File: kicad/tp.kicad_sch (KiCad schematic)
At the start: 11 parts, among them SW1 SWITCH_MODE, SW2 ALARM_OFF, U1 STM32F103RBTx

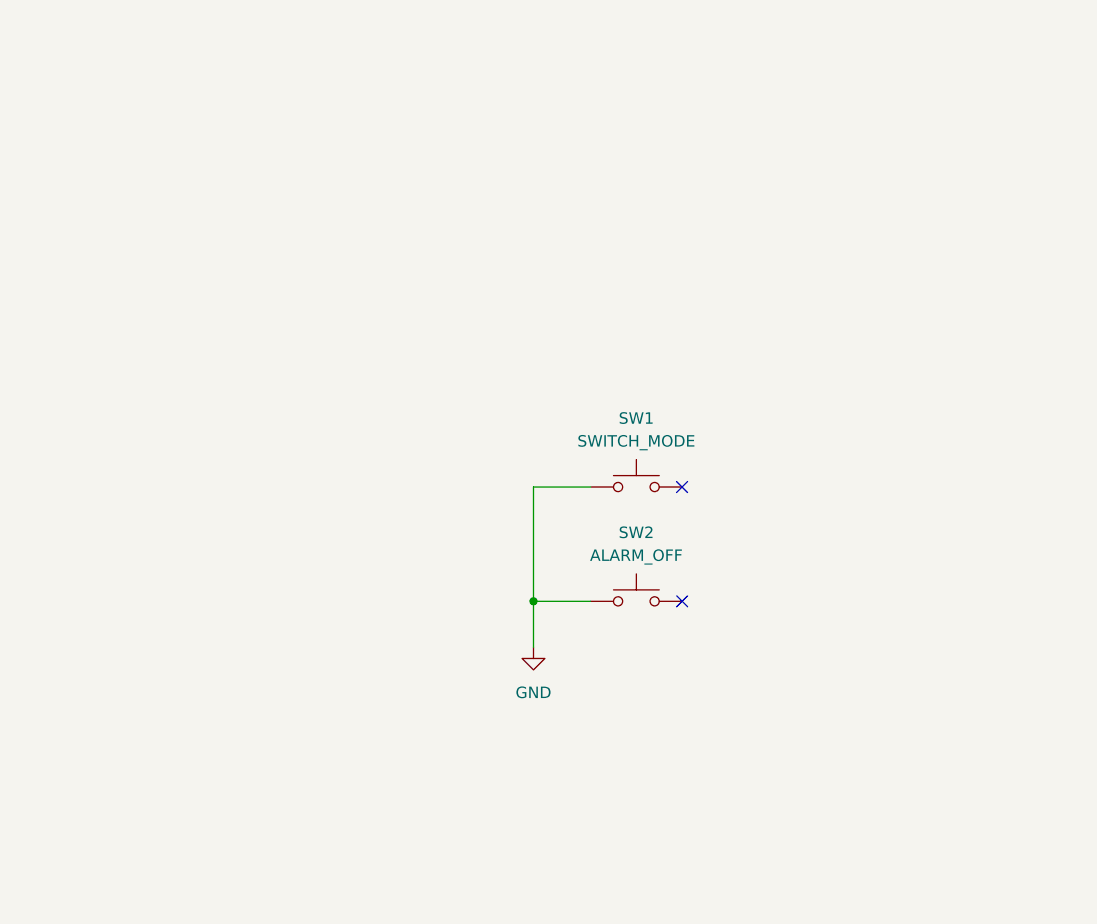
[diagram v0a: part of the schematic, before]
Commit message: feat(sch): agrega display lcd
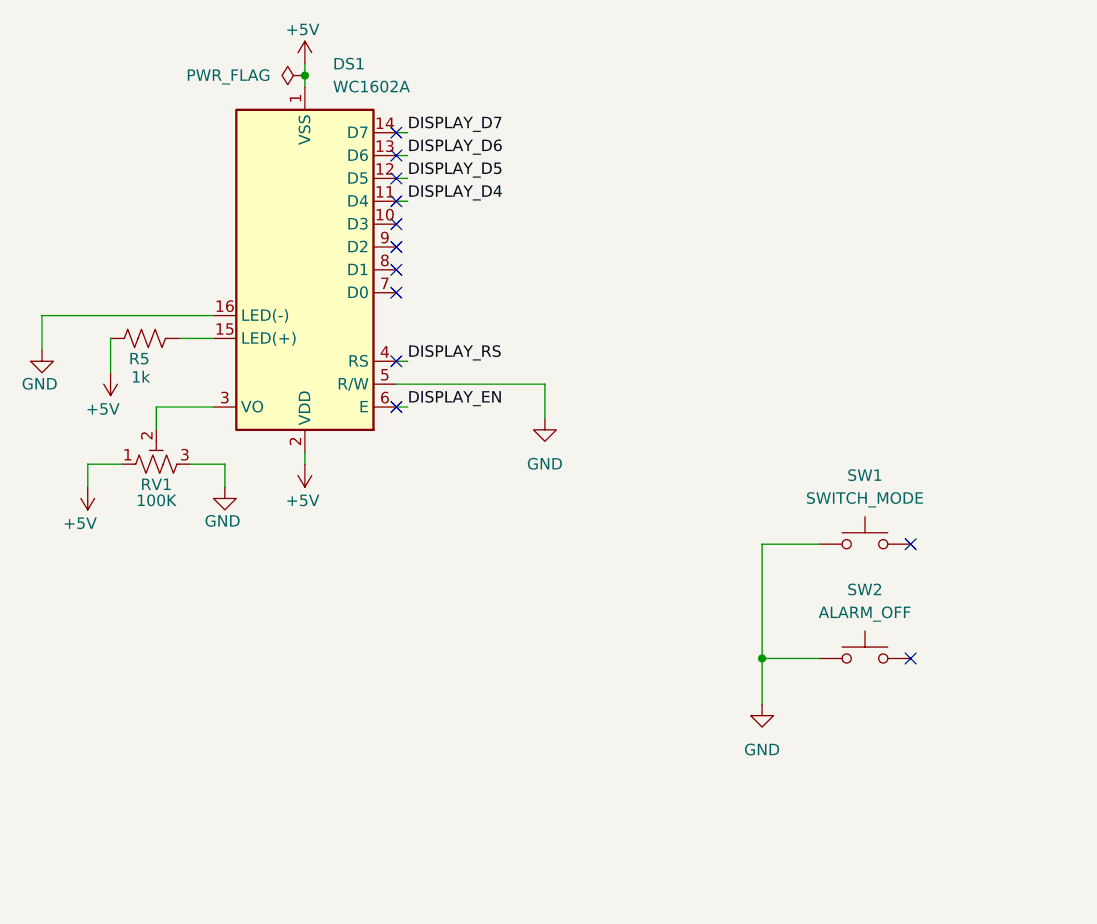
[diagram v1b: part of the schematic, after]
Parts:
- added DS1: WC1602A, Display:WC1602A, symbol Display_Character:WC1602A
- added R5: 1k, symbol Device:R_US
- added RV1: 100K, symbol Device:R_Potentiometer_Trim_US
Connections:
- net GND: now also DS1.16 (LED(-)), DS1.5 (R/W), RV1.3
- new net: DS1.15 (LED(+)), R5.1
- new net: DS1.3 (VO), RV1.2
- new net +5V: DS1.1 (VSS), DS1.2 (VDD), R5.2, RV1.1
- new net DISPLAY_D4: DS1.11 (D4)
- new net DISPLAY_D5: DS1.12 (D5)
- new net DISPLAY_D6: DS1.13 (D6)
- new net DISPLAY_D7: DS1.14 (D7)
- new net DISPLAY_EN: DS1.6 (E)
- new net DISPLAY_RS: DS1.4 (RS)
- no-connect marks 67 -> 77
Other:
- moved on the sheet: SW1, SW2

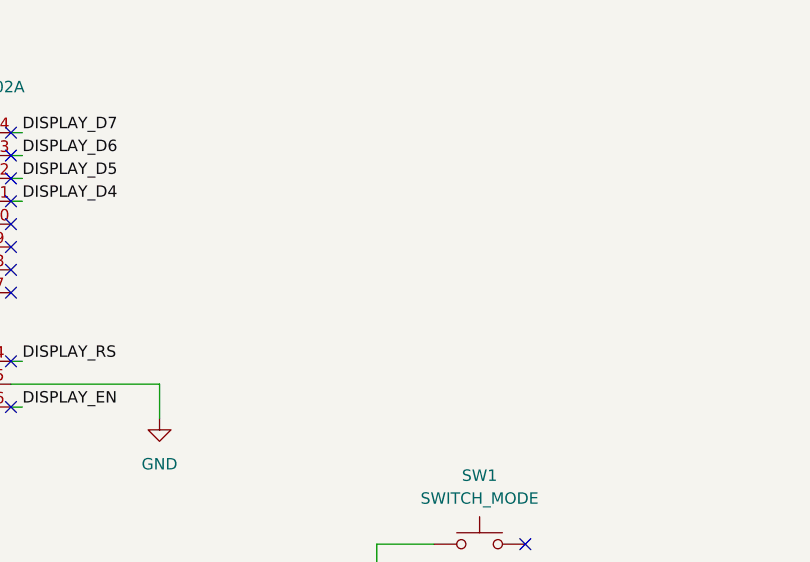
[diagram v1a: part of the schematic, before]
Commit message: feat(sch): agrega pines del hm10
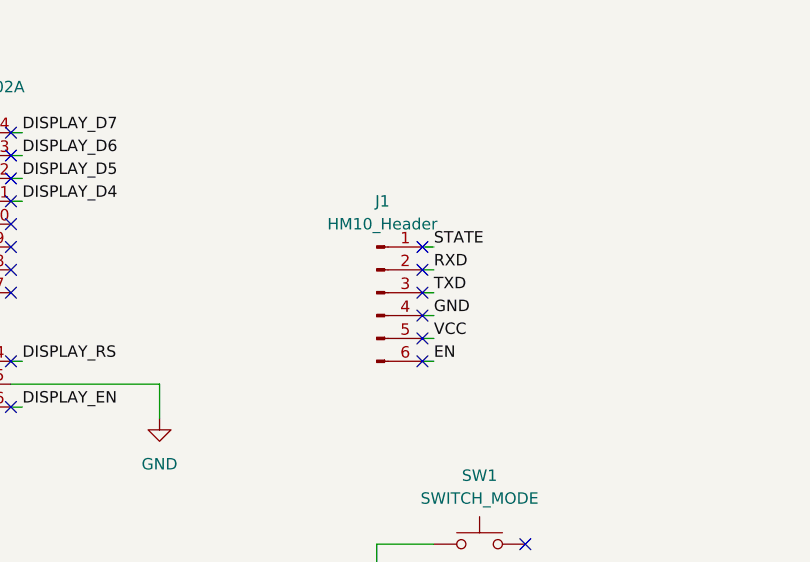
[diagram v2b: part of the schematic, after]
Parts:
- added J1: HM10_Header, symbol Connector:Conn_01x06_Pin
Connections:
- net GND: now also J1.4 (Pin_4)
- new net EN: J1.6 (Pin_6)
- new net RXD: J1.2 (Pin_2)
- new net STATE: J1.1 (Pin_1)
- new net TXD: J1.3 (Pin_3)
- new net VCC: J1.5 (Pin_5)
- no-connect marks 77 -> 83
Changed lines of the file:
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@@
+	)
+	(no_connect
+		(at 104.14 62.23)
 	)
 	(no_connect
@@
 	)
 	(no_connect
+		(at 104.14 52.07)
+	)
+	(no_connect
 		(at 184.15 109.22)
 	)
@@
 	)
 	(no_connect
+		(at 104.14 57.15)
+	)
+	(no_connect
 		(at 184.15 78.74)
 	)
@@
 	)
 	(no_connect
+		(at 104.14 49.53)
+	)
+	(no_connect
+		(at 104.14 59.69)
+	)
+	(no_connect
 		(at 184.15 99.06)
 	)
@@
 	)
 	(no_connect
+		(at 104.14 54.61)
+	)
+	(no_connect
 		(at 148.59 73.66)
 	)
@@
 	(wire
 		(pts
+			(xy 104.14 54.61) (xy 105.41 54.61)
+		)
+		(stroke
+			(width 0)
+			(type default)
+		)
+	)
+	(wire
+		(pts
 			(xy 31.75 67.31) (xy 38.1 67.31)
 		)
@@
 	(wire
 		(pts
+			(xy 104.14 57.15) (xy 105.41 57.15)
+		)
+		(stroke
+			(width 0)
+			(type default)
+		)
+	)
+	(wire
+		(pts
 			(xy 19.05 57.15) (xy 19.05 60.96)
 		)
@@
 	(wire
 		(pts
+			(xy 104.14 59.69) (xy 105.41 59.69)
+		)
+		(stroke
+			(width 0)
+			(type default)
+		)
+	)
+	(wire
+		(pts
 			(xy 219.71 88.9) (xy 224.79 88.9)
 		)
@@
 	(wire
 		(pts
+			(xy 104.14 52.07) (xy 105.41 52.07)
+		)
+		(stroke
+			(width 0)
+			(type default)
+		)
+	)
+	(wire
+		(pts
 			(xy 236.22 99.06) (xy 236.22 109.22)
 		)
@@
 	(wire
 		(pts
+			(xy 104.14 62.23) (xy 105.41 62.23)
+		)
+		(stroke
+			(width 0)
+			(type default)
+		)
+	)
+	(wire
+		(pts
 			(xy 58.42 44.45) (xy 59.69 44.45)
 		)
@@
 	(wire
 		(pts
+			(xy 105.41 49.53) (xy 104.14 49.53)
+		)
+		(stroke
+			(width 0)
+			(type default)
+		)
+	)
+	(wire
+		(pts
 			(xy 58.42 62.23) (xy 59.69 62.23)
 		)
@@
 			(width 0)
 			(type default)
+		)
+	)
+	(label "EN"
+		(at 105.41 62.23 0)
+		(effects
+			(font
+				(size 1.27 1.27)
+			)
+			(justify left bottom)
+		)
+	)
+	(label "GND"
+		(at 105.41 57.15 0)
+		(effects
+			(font
+				(size 1.27 1.27)
+			)
+			(justify left bottom)
+		)
+	)
+	(label "TXD"
+		(at 105.41 54.61 0)
+		(effects
+			(font
+				(size 1.27 1.27)
+			)
+			(justify left bottom)
+		)
+	)
+	(label "RXD"
+		(at 105.41 52.07 0)
+		(effects
+			(font
+				(size 1.27 1.27)
+			)
+			(justify left bottom)
 		)
 	)
@@
 		)
 	)
+	(label "STATE"
+		(at 105.41 49.53 0)
+		(effects
+			(font
+				(size 1.27 1.27)
+			)
+			(justify left bottom)
+		)
+	)
 	(label "DISPLAY_D4"
 		(at 59.69 44.45 0)
@@
 	(label "DISPLAY_EN"
 		(at 59.69 67.31 0)
+		(effects
+			(font
+				(size 1.27 1.27)
+			)
+			(justify left bottom)
+		)
+	)
+	(label "VCC"
+		(at 105.41 59.69 0)
 		(effects
 			(font
@@
 					(unit 1)
 				)
+			)
+		)
+	)
+	(symbol
+		(lib_id "Connector:Conn_01x06_Pin")
+		(at 99.06 54.61 0)
+		(unit 1)
+		(exclude_from_sim no)
+		(in_bom yes)
+		(on_board yes)
+		(dnp no)
+		(fields_autoplaced yes)
+		(property "Reference" "J1"
+			(at 99.695 44.45 0)
+			(effects
+				(font
+					(size 1.27 1.27)
+				)
+			)
+		)
+		(property "Value" "HM10_Header"
+			(at 99.695 46.99 0)
+			(effects
+				(font
+					(size 1.27 1.27)
+				)
+			)
+		)
+		(property "Footprint" ""
+			(at 99.06 54.61 0)
+			(effects
+				(font
+					(size 1.27 1.27)
+				)
+				(hide yes)
+			)
+		)
+		(property "Datasheet" "~"
+			(at 99.06 54.61 0)
+			(effects
+				(font
+					(size 1.27 1.27)
+				)
+				(hide yes)
+			)
+		)
+		(property "Description" "Generic connector, single row, 01x06, script generated"
+			(at 99.06 54.61 0)
+			(effects
+				(font
+					(size 1.27 1.27)
+				)
+				(hide yes)
+			)
+		)
+		(pin "2"
+		)
+		(pin "5"
+		)
+		(pin "4"
+		)
+		(pin "3"
+		)
+		(pin "1"
+		)
+		(pin "6"
+		)
+		(instances
+			(project ""
+				(path "/4321da81-5d44-4e9a-b537-a2876d1011a9"
+					(reference "J1")
+					(unit 1)
+				)

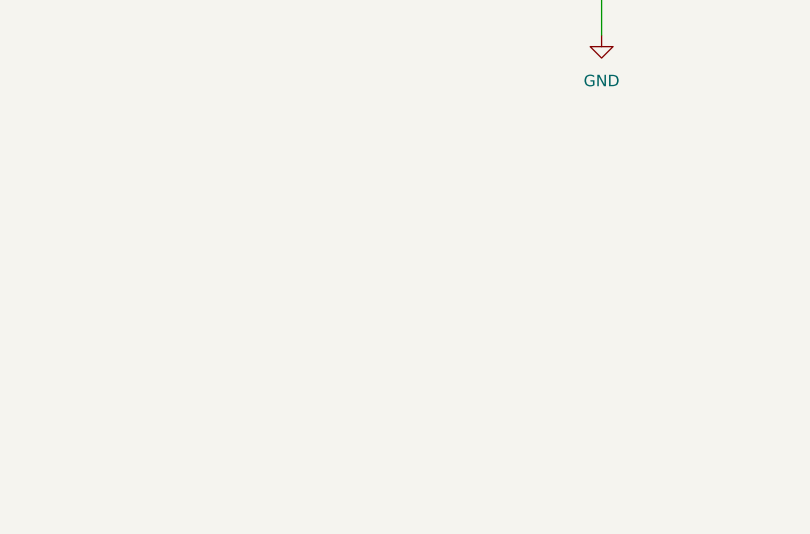
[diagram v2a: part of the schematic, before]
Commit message: feat(sch): agrega pines del max30102
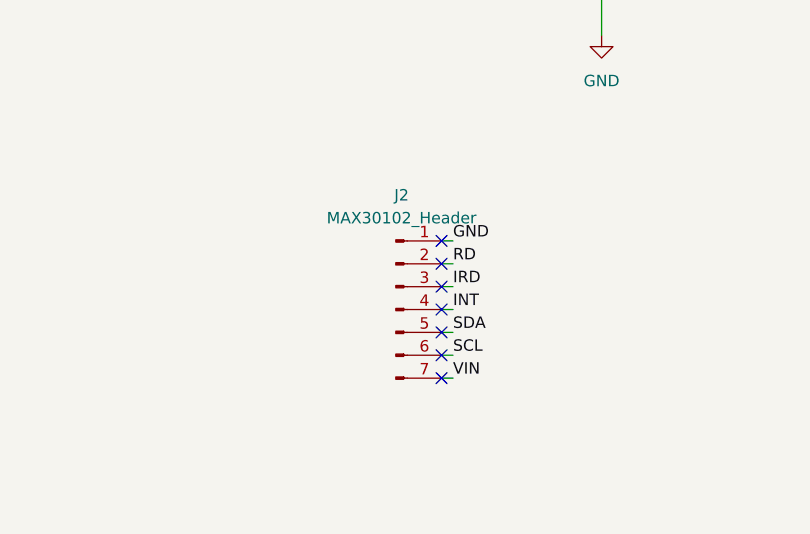
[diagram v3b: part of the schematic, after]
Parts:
- added J2: MAX30102_Header, symbol Connector:Conn_01x07_Pin
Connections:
- net GND: now also J2.1 (Pin_1)
- new net INT: J2.4 (Pin_4)
- new net IRD: J2.3 (Pin_3)
- new net RD: J2.2 (Pin_2)
- new net SCL: J2.6 (Pin_6)
- new net SDA: J2.5 (Pin_5)
- new net VIN: J2.7 (Pin_7)
- no-connect marks 83 -> 90
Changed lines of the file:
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@@
+	)
+	(no_connect
+		(at 81.28 130.81)
 	)
 	(no_connect
@@
 	)
 	(no_connect
+		(at 81.28 128.27)
+	)
+	(no_connect
+		(at 81.28 135.89)
+	)
+	(no_connect
 		(at 148.59 71.12)
 	)
@@
 	)
 	(no_connect
+		(at 81.28 125.73)
+	)
+	(no_connect
 		(at 148.59 96.52)
 	)
@@
 	)
 	(no_connect
+		(at 81.28 138.43)
+	)
+	(no_connect
 		(at 148.59 119.38)
 	)
@@
 	)
 	(no_connect
+		(at 81.28 123.19)
+	)
+	(no_connect
 		(at 184.15 73.66)
 	)
@@
 	)
 	(no_connect
+		(at 81.28 133.35)
+	)
+	(no_connect
 		(at 184.15 91.44)
 	)
@@
 	(wire
 		(pts
+			(xy 82.55 123.19) (xy 81.28 123.19)
+		)
+		(stroke
+			(width 0)
+			(type default)
+		)
+	)
+	(wire
+		(pts
 			(xy 105.41 82.55) (xy 99.06 82.55)
 		)
@@
 	(wire
 		(pts
+			(xy 81.28 130.81) (xy 82.55 130.81)
+		)
+		(stroke
+			(width 0)
+			(type default)
+		)
+	)
+	(wire
+		(pts
+			(xy 81.28 125.73) (xy 82.55 125.73)
+		)
+		(stroke
+			(width 0)
+			(type default)
+		)
+	)
+	(wire
+		(pts
+			(xy 81.28 128.27) (xy 82.55 128.27)
+		)
+		(stroke
+			(width 0)
+			(type default)
+		)
+	)
+	(wire
+		(pts
 			(xy 219.71 109.22) (xy 223.52 109.22)
 		)
@@
 	(wire
 		(pts
+			(xy 81.28 138.43) (xy 82.55 138.43)
+		)
+		(stroke
+			(width 0)
+			(type default)
+		)
+	)
+	(wire
+		(pts
 			(xy 232.41 88.9) (xy 236.22 88.9)
 		)
@@
 	(wire
 		(pts
+			(xy 81.28 133.35) (xy 82.55 133.35)
+		)
+		(stroke
+			(width 0)
+			(type default)
+		)
+	)
+	(wire
+		(pts
 			(xy 31.75 69.85) (xy 31.75 67.31)
 		)
@@
 		(pts
 			(xy 39.37 73.66) (xy 39.37 76.2)
+		)
+		(stroke
+			(width 0)
+			(type default)
+		)
+	)
+	(wire
+		(pts
+			(xy 81.28 135.89) (xy 82.55 135.89)
 		)
 		(stroke
@@
 		)
 	)
+	(label "SDA"
+		(at 82.55 133.35 0)
+		(effects
+			(font
+				(size 1.27 1.27)
+			)
+			(justify left bottom)
+		)
+	)
 	(label "GND"
 		(at 105.41 57.15 0)
@@
 		)
 	)
+	(label "VIN"
+		(at 82.55 138.43 0)
+		(effects
+			(font
+				(size 1.27 1.27)
+			)
+			(justify left bottom)
+		)
+	)
 	(label "DISPLAY_EN"
 		(at 59.69 67.31 0)
@@
 		)
 	)
+	(label "RD"
+		(at 82.55 125.73 0)
+		(effects
+			(font
+				(size 1.27 1.27)
+			)
+			(justify left bottom)
+		)
+	)
 	(label "VCC"
 		(at 105.41 59.69 0)
@@
 		)
 	)
+	(label "INT"
+		(at 82.55 130.81 0)
+		(effects
+			(font
+				(size 1.27 1.27)
+			)
+			(justify left bottom)
+		)
+	)
+	(label "IRD"
+		(at 82.55 128.27 0)
+		(effects
+			(font
+				(size 1.27 1.27)
+			)
+			(justify left bottom)
+		)
+	)
 	(label "DISPLAY_D6"
 		(at 59.69 39.37 0)
@@
 	(label "DISPLAY_D7"
 		(at 59.69 36.83 0)
+		(effects
+			(font
+				(size 1.27 1.27)
+			)
+			(justify left bottom)
+		)
+	)
+	(label "GND"
+		(at 82.55 123.19 0)
+		(effects
+			(font
+				(size 1.27 1.27)
+			)
+			(justify left bottom)
+		)
+	)
+	(label "SCL"
+		(at 82.55 135.89 0)
 		(effects
 			(font
@@
 					(unit 1)
 				)
+			)
+		)
+	)
+	(symbol
+		(lib_id "Connector:Conn_01x07_Pin")
+		(at 76.2 130.81 0)
+		(unit 1)
+		(exclude_from_sim no)
+		(in_bom yes)
+		(on_board yes)
+		(dnp no)
+		(fields_autoplaced yes)
+		(property "Reference" "J2"
+			(at 76.835 118.11 0)
+			(effects
+				(font
+					(size 1.27 1.27)
+				)
+			)
+		)
+		(property "Value" "MAX30102_Header"
+			(at 76.835 120.65 0)
+			(effects
+				(font
+					(size 1.27 1.27)
+				)
+			)
+		)
+		(property "Footprint" ""
+			(at 76.2 130.81 0)
+			(effects
+				(font
+					(size 1.27 1.27)
+				)
+				(hide yes)
+			)
+		)
+		(property "Datasheet" "~"
+			(at 76.2 130.81 0)
+			(effects
+				(font
+					(size 1.27 1.27)
+				)
+				(hide yes)
+			)
+		)
+		(property "Description" "Generic connector, single row, 01x07, script generated"
+			(at 76.2 130.81 0)
+			(effects
+				(font
+					(size 1.27 1.27)
+				)
+				(hide yes)
+			)
+		)
+		(pin "2"
+		)
+		(pin "5"
+		)
+		(pin "4"
+		)
+		(pin "3"
+		)
+		(pin "1"
+		)
+		(pin "6"
+		)
+		(pin "7"
+		)
+		(instances
+			(project "tp"
+				(path "/4321da81-5d44-4e9a-b537-a2876d1011a9"
+					(reference "J2")
+					(unit 1)
+				)
